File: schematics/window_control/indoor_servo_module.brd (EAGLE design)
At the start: 48.2 x 59.4 mm, 29 parts, among them J1 MTR-SERVO-FS5103B, J2 JST-XH2.54-4P, J3 JST-XH2.54-2P, J4 JST-XH2.54-3P, Q2 2N3904, Q3 2N3906BU, Q4 2N3904, Q5 STP14NM50N, SW1 SWITCH, U2 LM311P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

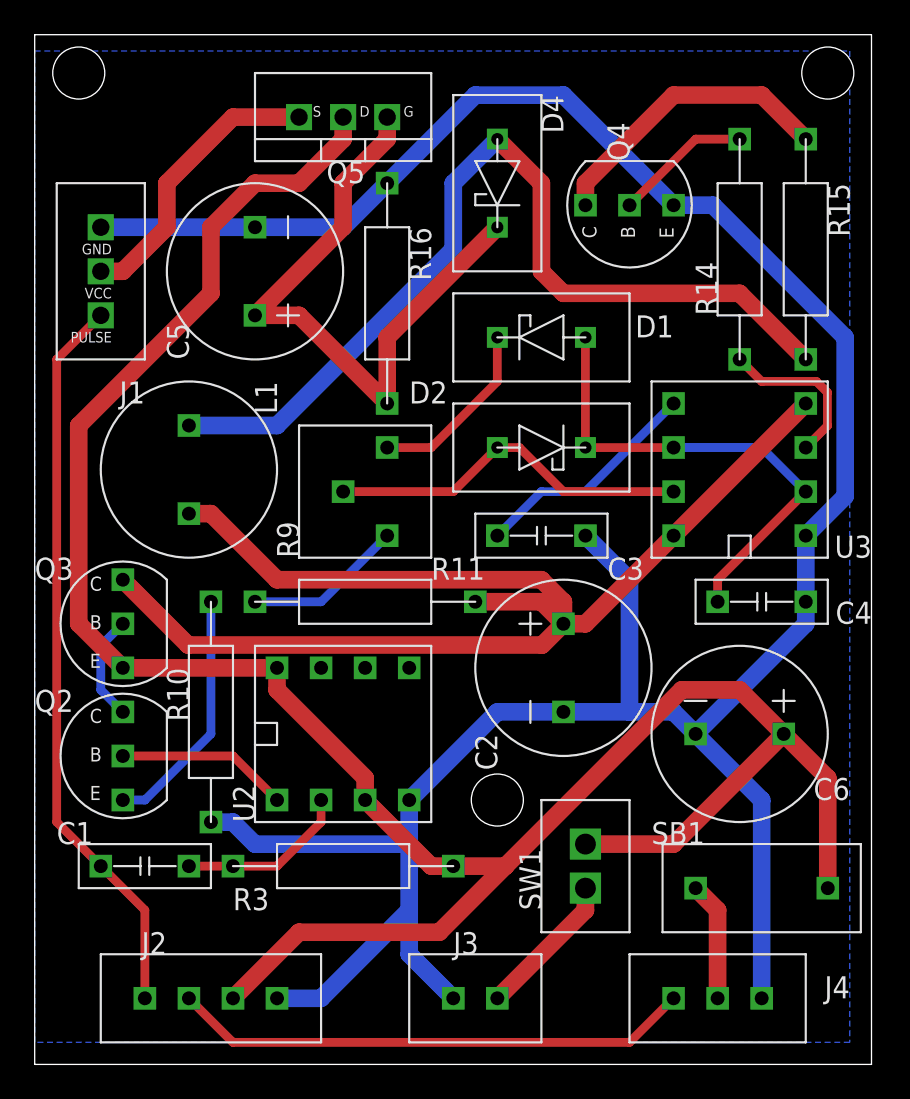
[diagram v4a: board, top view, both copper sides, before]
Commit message: Increased supply line size to servo
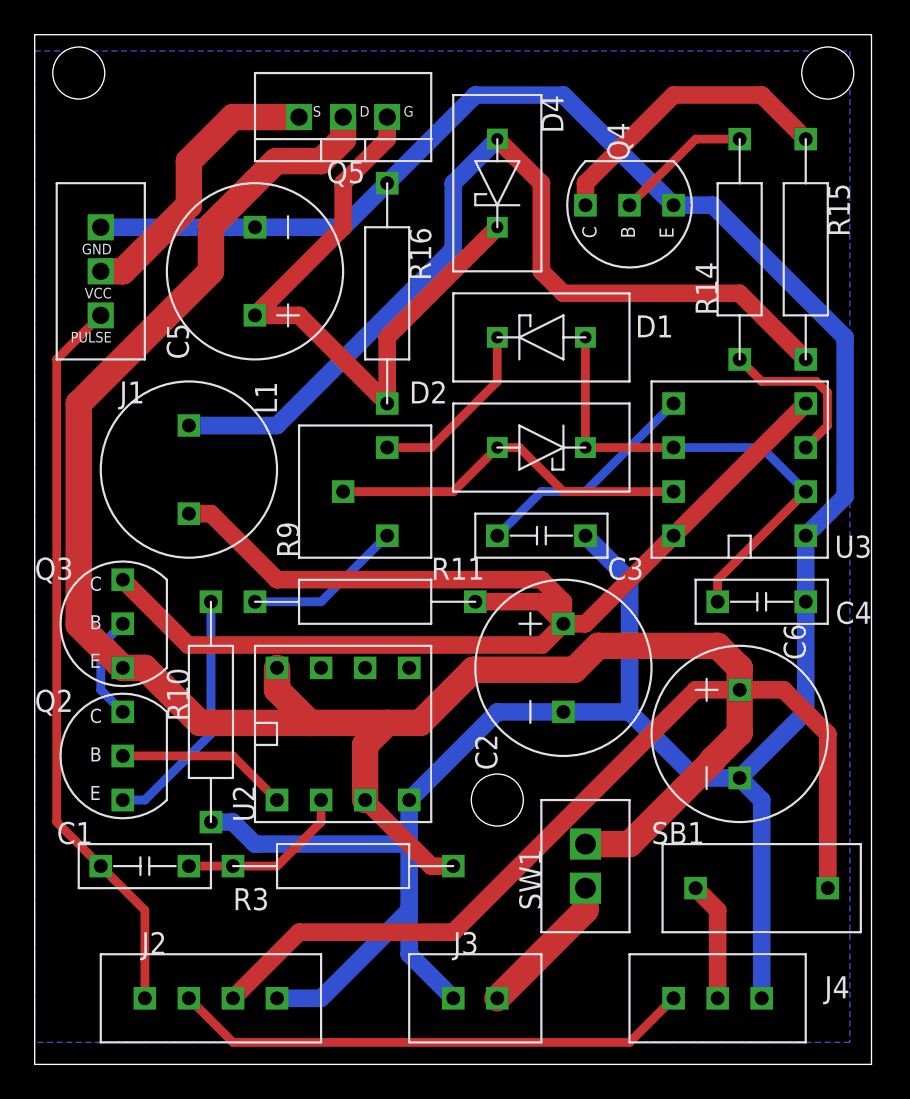
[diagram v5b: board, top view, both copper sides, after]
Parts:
- turned C6 to 270 degrees
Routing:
- net +5V: track 133.1 -> 162.4 mm
- net GND: track 159.6 -> 161.1 mm
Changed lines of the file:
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@@
 <attribute name="NAME" x="85.09" y="21.59" size="1.27" layer="21" rot="R180"/>
 </element>
-<element name="C6" library="my_devices" package="C" value="1000 uF" x="77.47" y="10.16" smashed="yes" rot="R180">
-<attribute name="NAME" x="83.82" y="7.62" size="1.27" layer="21" rot="R180"/>
+<element name="C6" library="my_devices" package="C" value="1000 uF" x="77.47" y="10.16" smashed="yes" rot="R270">
+<attribute name="NAME" x="80.01" y="16.51" size="1.27" layer="21" rot="R270"/>
 </element>
 <element name="D1" library="my_devices" package="D_SCHOTTKY" value="BAT41" x="66.04" y="33.02" smashed="yes" rot="R180">
@@
 <contactref element="SB1" pad="P$2"/>
 <contactref element="C6" pad="PIN_PLUS"/>
-<wire x1="82.55" y1="1.27" x2="82.55" y2="7.62" width="1.016" layer="1"/>
-<wire x1="82.55" y1="7.62" x2="80.01" y2="10.16" width="1.016" layer="1"/>
-<wire x1="68.58" y1="3.81" x2="73.66" y2="3.81" width="1.016" layer="1"/>
-<wire x1="73.66" y1="3.81" x2="80.01" y2="10.16" width="1.016" layer="1"/>
-<wire x1="55.88" y1="6.35" x2="55.88" y2="7.62" width="1.016" layer="1"/>
-<wire x1="50.8" y1="12.7" x2="50.8" y2="13.97" width="1.016" layer="1"/>
-<wire x1="55.88" y1="7.62" x2="50.8" y2="12.7" width="1.016" layer="1"/>
-<wire x1="50.8" y1="13.97" x2="41.91" y2="13.97" width="1.016" layer="1"/>
-<wire x1="41.91" y1="13.97" x2="39.37" y2="16.51" width="1.016" layer="1"/>
-<wire x1="39.37" y1="16.51" x2="39.37" y2="27.94" width="1.016" layer="1"/>
-<wire x1="46.99" y1="35.56" x2="46.99" y2="39.37" width="1.016" layer="1"/>
-<wire x1="46.99" y1="39.37" x2="49.53" y2="41.91" width="1.016" layer="1"/>
-<wire x1="49.53" y1="41.91" x2="52.07" y2="41.91" width="1.016" layer="1"/>
-<wire x1="52.07" y1="41.91" x2="54.61" y2="44.45" width="1.016" layer="1"/>
-<wire x1="54.61" y1="44.45" x2="54.61" y2="45.72" width="1.016" layer="1"/>
-<wire x1="39.37" y1="27.94" x2="46.99" y2="35.56" width="1.016" layer="1"/>
+<wire x1="82.55" y1="1.27" x2="82.55" y2="10.16" width="1.016" layer="1"/>
 <contactref element="J2" pad="PIN2"/>
-<wire x1="77.47" y1="12.7" x2="80.01" y2="10.16" width="1.016" layer="1"/>
-<wire x1="77.47" y1="12.7" x2="74.1265875" y2="12.7" width="1.016" layer="1"/>
-<wire x1="63.9665875" y1="2.54" x2="60.96" y2="2.54" width="1.016" layer="1"/>
-<wire x1="74.1265875" y1="12.7" x2="63.9665875" y2="2.54" width="1.016" layer="1"/>
 <wire x1="60.96" y1="2.54" x2="59.69" y2="2.54" width="1.016" layer="1"/>
 <wire x1="59.69" y1="2.54" x2="55.88" y2="6.35" width="1.016" layer="1"/>
 <wire x1="48.26" y1="-5.08" x2="52.07" y2="-1.27" width="1.016" layer="1"/>
-<wire x1="60.1565875" y1="-1.27" x2="63.9665875" y2="2.54" width="1.016" layer="1"/>
-<wire x1="52.07" y1="-1.27" x2="60.1565875" y2="-1.27" width="1.016" layer="1"/>
+<wire x1="52.07" y1="-1.27" x2="60.96" y2="-1.27" width="1.016" layer="1"/>
+<wire x1="82.55" y1="10.16" x2="80.01" y2="12.7" width="1.016" layer="1"/>
+<wire x1="80.01" y1="12.7" x2="77.47" y2="12.7" width="1.016" layer="1"/>
+<wire x1="74.93" y1="12.7" x2="77.47" y2="12.7" width="1.016" layer="1"/>
+<wire x1="60.96" y1="-1.27" x2="74.93" y2="12.7" width="1.016" layer="1"/>
+<wire x1="68.58" y1="3.81" x2="71.12" y2="3.81" width="1.524" layer="1"/>
+<wire x1="71.12" y1="3.81" x2="75.9016" y2="8.5916" width="1.524" layer="1"/>
+<wire x1="75.9016" y1="8.5916" x2="75.9016" y2="8.65275625" width="1.524" layer="1"/>
+<wire x1="77.47" y1="10.22115625" x2="77.47" y2="12.7" width="1.524" layer="1"/>
+<wire x1="75.9016" y1="8.65275625" x2="77.47" y2="10.22115625" width="1.524" layer="1"/>
+<wire x1="77.47" y1="12.7" x2="77.47" y2="13.97" width="1.524" layer="1"/>
+<wire x1="77.47" y1="13.97" x2="76.2" y2="15.24" width="1.524" layer="1"/>
+<wire x1="69.32158125" y1="15.24" x2="67.94358125" y2="13.862" width="1.524" layer="1"/>
+<wire x1="62.122" y1="13.862" x2="67.94358125" y2="13.862" width="1.524" layer="1"/>
+<wire x1="76.2" y1="15.24" x2="69.32158125" y2="15.24" width="1.524" layer="1"/>
+<wire x1="41.91" y1="13.97" x2="40.9384" y2="14.9416" width="1.524" layer="1"/>
+<wire x1="40.9384" y1="14.9416" x2="40.87724375" y2="14.9416" width="1.524" layer="1"/>
+<wire x1="40.87724375" y1="14.9416" x2="39.37" y2="16.44884375" width="1.524" layer="1"/>
+<wire x1="46.99" y1="39.43115625" x2="50.73884375" y2="43.18" width="1.524" layer="1"/>
+<wire x1="53.34" y1="43.18" x2="54.61" y2="44.45" width="1.524" layer="1"/>
+<wire x1="54.61" y1="44.45" x2="54.61" y2="45.72" width="1.524" layer="1"/>
+<wire x1="39.37" y1="16.44884375" x2="39.37" y2="29.21" width="1.524" layer="1"/>
+<wire x1="39.37" y1="29.21" x2="46.99" y2="36.83" width="1.524" layer="1"/>
+<wire x1="46.99" y1="36.83" x2="46.99" y2="39.43115625" width="1.524" layer="1"/>
+<wire x1="50.73884375" y1="43.18" x2="53.34" y2="43.18" width="1.524" layer="1"/>
+<wire x1="41.91" y1="13.97" x2="43.18" y2="13.97" width="1.524" layer="1"/>
+<wire x1="46.355" y1="10.795" x2="52.705" y2="10.795" width="1.524" layer="1"/>
+<wire x1="43.18" y1="13.97" x2="46.355" y2="10.795" width="1.524" layer="1"/>
+<wire x1="52.705" y1="10.795" x2="57.15" y2="10.795" width="1.524" layer="1"/>
+<wire x1="57.15" y1="10.795" x2="59.055" y2="10.795" width="1.524" layer="1"/>
+<wire x1="59.055" y1="10.795" x2="62.122" y2="13.862" width="1.524" layer="1"/>
+<wire x1="50.8" y1="13.97" x2="50.8" y2="12.7" width="1.524" layer="1"/>
+<wire x1="50.8" y1="12.7" x2="52.705" y2="10.795" width="1.524" layer="1"/>
+<wire x1="55.88" y1="9.525" x2="57.15" y2="10.795" width="1.524" layer="1"/>
+<wire x1="55.88" y1="6.35" x2="55.88" y2="9.525" width="1.524" layer="1"/>
 </signal>
 <signal name="GND">
@@
 <wire x1="48.26" y1="5.08" x2="49.53" y2="3.81" width="1.016" layer="16"/>
 <wire x1="49.53" y1="3.81" x2="58.42" y2="3.81" width="1.016" layer="16"/>
-<wire x1="74.93" y1="10.16" x2="81.28" y2="16.51" width="1.016" layer="16"/>
-<wire x1="81.28" y1="17.78" x2="81.28" y2="16.51" width="1.016" layer="16"/>
 <wire x1="81.28" y1="17.78" x2="81.28" y2="21.59" width="1.016" layer="16"/>
 <wire x1="57.15" y1="41.91" x2="54.61" y2="39.37" width="1.016" layer="16"/>
@@
 <wire x1="63.5" y1="11.43" x2="67.31" y2="11.43" width="1.016" layer="16"/>
 <wire x1="67.31" y1="11.43" x2="71.12" y2="11.43" width="1.016" layer="16"/>
-<wire x1="71.12" y1="11.43" x2="73.66" y2="11.43" width="1.016" layer="16"/>
-<wire x1="73.66" y1="11.43" x2="74.93" y2="10.16" width="1.016" layer="16"/>
 <wire x1="68.58" y1="21.59" x2="71.12" y2="19.05" width="1.016" layer="16"/>
 <wire x1="71.12" y1="19.05" x2="71.12" y2="11.43" width="1.016" layer="16"/>
@@
 <wire x1="58.42" y1="0" x2="58.42" y2="-2.54" width="1.016" layer="16"/>
 <wire x1="58.42" y1="-2.54" x2="60.96" y2="-5.08" width="1.016" layer="16"/>
-<wire x1="74.93" y1="10.16" x2="78.74" y2="6.35" width="1.016" layer="16"/>
-<wire x1="78.74" y1="6.35" x2="78.74" y2="-5.08" width="1.016" layer="16"/>
+<wire x1="78.74" y1="-5.08" x2="78.74" y2="6.35" width="1.016" layer="16"/>
+<wire x1="78.74" y1="6.35" x2="77.47" y2="7.62" width="1.016" layer="16"/>
+<wire x1="77.47" y1="7.62" x2="81.28" y2="11.43" width="1.016" layer="16"/>
+<wire x1="81.28" y1="11.43" x2="81.28" y2="17.78" width="1.016" layer="16"/>
+<wire x1="77.47" y1="7.62" x2="74.93" y2="7.62" width="1.016" layer="16"/>
+<wire x1="74.93" y1="7.62" x2="71.12" y2="11.43" width="1.016" layer="16"/>
 </signal>
 <signal name="SERVO_PWM_CONTROL">
@@
 <contactref element="J1" pad="VCC"/>
 <contactref element="Q5" pad="S"/>
-<wire x1="40.64" y1="36.83" x2="41.91" y2="36.83" width="1.016" layer="1"/>
-<wire x1="41.91" y1="36.83" x2="44.45" y2="39.37" width="1.016" layer="1"/>
-<wire x1="44.45" y1="39.37" x2="44.45" y2="41.91" width="1.016" layer="1"/>
-<wire x1="44.45" y1="41.91" x2="48.26" y2="45.72" width="1.016" layer="1"/>
-<wire x1="48.26" y1="45.72" x2="52.07" y2="45.72" width="1.016" layer="1"/>
+<wire x1="40.64" y1="36.83" x2="41.91" y2="36.83" width="1.524" layer="1"/>
+<wire x1="41.91" y1="36.83" x2="45.72" y2="40.64" width="1.524" layer="1"/>
+<wire x1="45.72" y1="40.64" x2="45.72" y2="43.18" width="1.524" layer="1"/>
+<wire x1="45.72" y1="43.18" x2="48.26" y2="45.72" width="1.524" layer="1"/>
+<wire x1="48.26" y1="45.72" x2="52.07" y2="45.72" width="1.524" layer="1"/>
 </signal>
 <signal name="N$44">
@@
 <contactref element="SW1" pad="P$1"/>
 <contactref element="J3" pad="PIN2"/>
-<wire x1="68.58" y1="1.27" x2="68.58" y2="0" width="1.016" layer="1"/>
-<wire x1="68.58" y1="0" x2="63.5" y2="-5.08" width="1.016" layer="1"/>
+<wire x1="63.5" y1="-5.08" x2="68.58" y2="0" width="1.524" layer="1"/>
+<wire x1="68.58" y1="0" x2="68.58" y2="1.27" width="1.524" layer="1"/>
 </signal>
 <signal name="N$4">

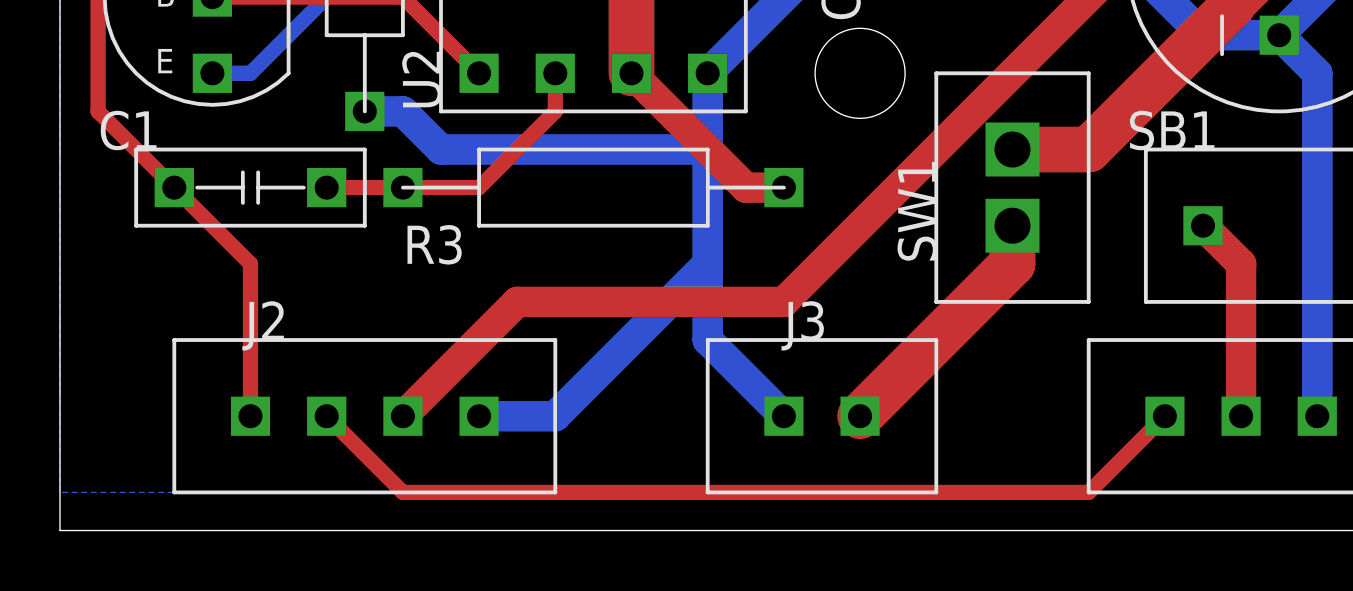
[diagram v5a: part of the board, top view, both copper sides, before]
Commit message: Outdoor module board size reduced
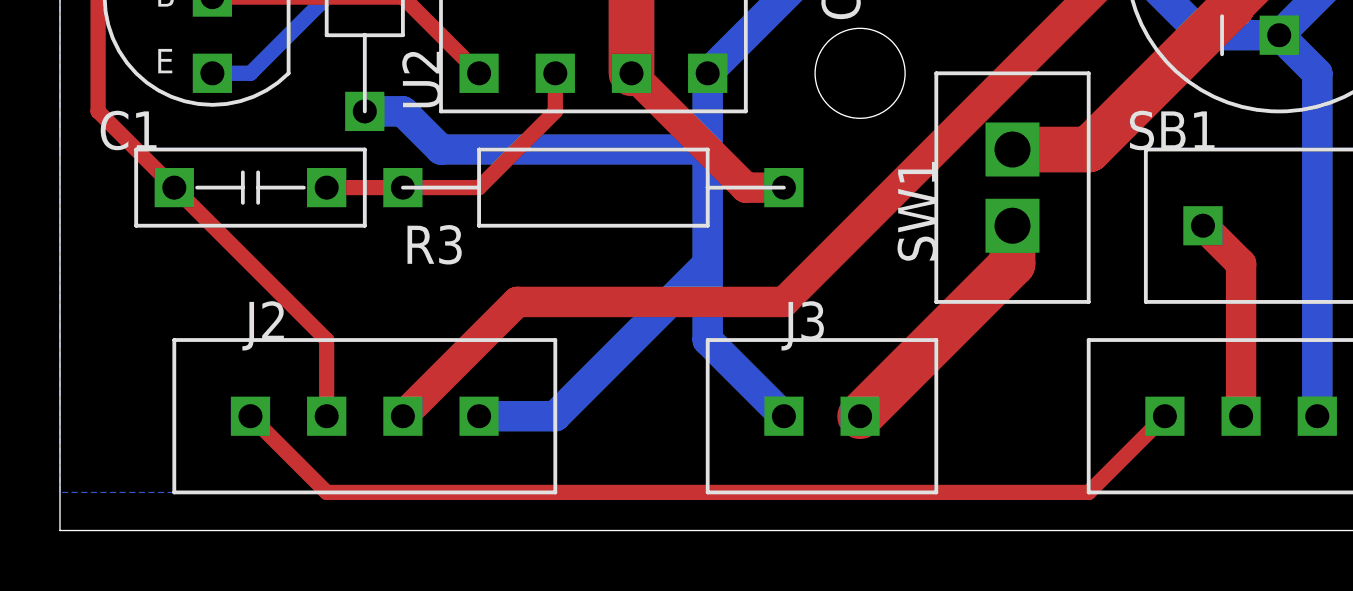
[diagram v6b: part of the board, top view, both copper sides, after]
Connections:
- net OUTDOOR_SIGNAL: now also J2.PIN4; no longer J2.PIN3
- net SERVO_PWM_CONTROL: now also J2.PIN3; no longer J2.PIN4
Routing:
- net OUTDOOR_SIGNAL: track 30.0 -> 32.6 mm
- net SERVO_PWM_CONTROL: track 42.5 -> 43.6 mm
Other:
- board text added: "+5V"
- board text added: "GND"
- board text added: "PWM"
- board text added: "SGN"
- board text added: "VCC"
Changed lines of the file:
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@@
 <hole x="82.55" y="48.26" drill="3"/>
 <hole x="63.5" y="6.35" drill="3"/>
+<text x="54.61" y="-7.62" size="1.778" layer="26" rot="MR0">GND</text>
+<text x="62.23" y="-7.62" size="1.778" layer="26" rot="MR0">GND</text>
+<text x="68.58" y="-7.62" size="1.778" layer="26" rot="MR0">+5V</text>
+<text x="83.82" y="-7.62" size="1.778" layer="26" rot="MR0">GND</text>
+<text x="77.47" y="-7.62" size="1.778" layer="26" rot="MR0">+5V</text>
+<text x="73.66" y="-3.81" size="1.778" layer="26" rot="MR0">SGN</text>
+<text x="50.8" y="-3.81" size="1.778" layer="26" rot="MR0">+5V</text>
+<text x="46.99" y="-7.62" size="1.778" layer="26" rot="MR0">PWM</text>
+<text x="43.18" y="-3.81" size="1.778" layer="26" rot="MR0">SGN</text>
+<text x="46.99" y="38.1" size="1.778" layer="26" rot="MR0">GND</text>
+<text x="46.99" y="35.56" size="1.778" layer="26" rot="MR0">VCC</text>
+<text x="48.26" y="33.02" size="1.778" layer="26" rot="MR0">PWM</text>
 </plain>
 <attributes>
@@
 <wire x1="38.1" y1="5.08" x2="38.1" y2="31.75" width="0.508" layer="1"/>
 <wire x1="38.1" y1="31.75" x2="40.64" y2="34.29" width="0.508" layer="1"/>
-<contactref element="J2" pad="PIN4"/>
-<wire x1="40.64" y1="2.54" x2="43.18" y2="0" width="0.508" layer="1"/>
-<wire x1="43.18" y1="0" x2="43.18" y2="-5.08" width="0.508" layer="1"/>
+<contactref element="J2" pad="PIN3"/>
+<wire x1="45.72" y1="-2.54" x2="45.72" y2="-5.08" width="0.508" layer="1"/>
+<wire x1="40.64" y1="2.54" x2="45.72" y2="-2.54" width="0.508" layer="1"/>
 </signal>
 <signal name="N$39">
@@
 <signal name="OUTDOOR_SIGNAL">
 <contactref element="J4" pad="PIN3"/>
-<contactref element="J2" pad="PIN3"/>
-<wire x1="45.72" y1="-5.08" x2="48.26" y2="-7.62" width="0.508" layer="1"/>
-<wire x1="71.12" y1="-7.62" x2="73.66" y2="-5.08" width="0.508" layer="1"/>
-<wire x1="48.26" y1="-7.62" x2="71.12" y2="-7.62" width="0.508" layer="1"/>
+<wire x1="73.66" y1="-5.08" x2="71.12" y2="-7.62" width="0.508" layer="1"/>
+<contactref element="J2" pad="PIN4"/>
+<wire x1="45.72" y1="-7.62" x2="43.18" y2="-5.08" width="0.508" layer="1"/>
+<wire x1="71.12" y1="-7.62" x2="45.72" y2="-7.62" width="0.508" layer="1"/>
 </signal>
 <signal name="N$3">
